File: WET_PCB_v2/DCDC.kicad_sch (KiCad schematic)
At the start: 5 parts, among them Q5 Q_NMOS_GDS, Q6 Q_NMOS_GDS

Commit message: notees
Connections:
- net DCDC_coil_circuit_side: no longer Q5.2 (D), Q6.2 (D)
- net VoutDCDC: now also Q6.2 (D); no longer Q6.3 (S)
- new net Gatedriver/Vs_node: Q5.2 (D), Q6.3 (S)
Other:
- note added: "curr sense points"
- moved on the sheet: Q6
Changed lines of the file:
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@@
+		)
+	)
+	(text "curr sense points"
+		(exclude_from_sim no)
+		(at 82.296 42.926 0)
+		(effects
+			(font
+				(size 1.27 1.27)
+			)
 		)
 	)
@@
 			)
 		)
-	)
-	(junction
-		(at 72.39 43.18)
-		(diameter 0)
-		(color 0 0 0 0)
 	)
 	(junction
@@
 		(color 0 0 0 0)
 	)
-	(junction
-		(at 91.44 43.18)
-		(diameter 0)
-		(color 0 0 0 0)
-	)
 	(wire
 		(pts
@@
 		(pts
 			(xy 72.39 52.07) (xy 72.39 43.18)
-		)
-		(stroke
-			(width 0)
-			(type default)
-		)
-	)
-	(wire
-		(pts
-			(xy 72.39 43.18) (xy 91.44 43.18)
 		)
 		(stroke
@@
 	(symbol
 		(lib_id "Transistor_FET:Q_NMOS_GDS")
-		(at 119.38 45.72 90)
+		(at 119.38 45.72 270)
+		(mirror x)
 		(unit 1)
 		(body_style 1)
@@
 		)
 		(property "Footprint" "Package_TO_SOT_THT:TO-220-3_Vertical"
-			(at 116.84 40.64 0)
-			(hide yes)
-			(show_name no)
+			(at 121.92 40.64 0)
+			(hide yes)
+			(show_name no)

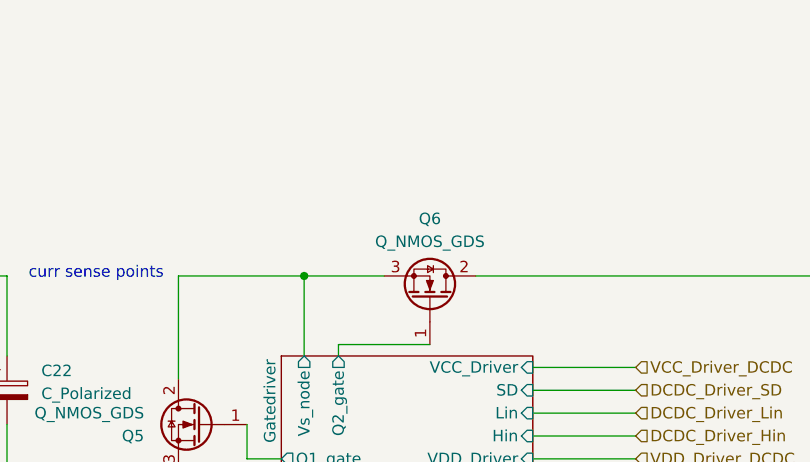
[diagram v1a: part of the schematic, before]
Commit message: redid part of layout inverter
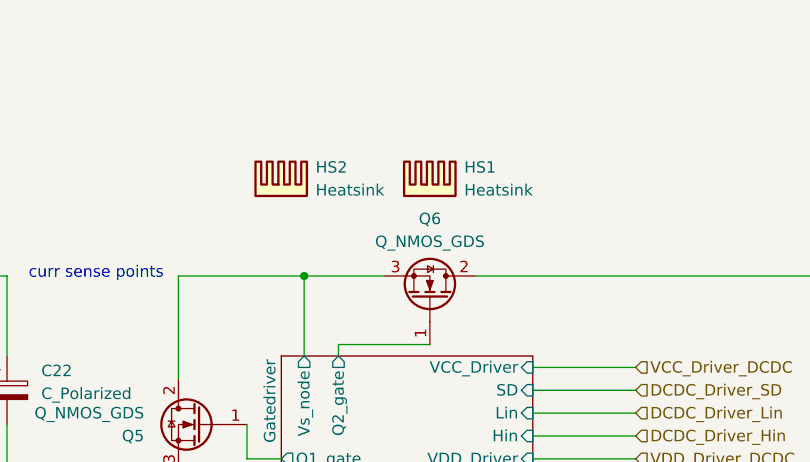
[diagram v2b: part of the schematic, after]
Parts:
- added HS1, HS2: Heatsink, Heatsink:Heatsink_AAVID_Extruded_531002B02100G_34.9x12.7mm_H25.4mm, symbol Mechanical:Heatsink
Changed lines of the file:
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@@
+	)
+	(symbol
+		(lib_id "Mechanical:Heatsink")
+		(at 119.38 34.29 0)
+		(unit 1)
+		(body_style 1)
+		(exclude_from_sim no)
+		(in_bom yes)
+		(on_board yes)
+		(in_pos_files yes)
+		(dnp no)
+		(fields_autoplaced yes)
+		(property "Reference" "HS1"
+			(at 123.19 31.1149 0)
+			(show_name no)
+			(do_not_autoplace no)
+			(effects
+				(font
+					(size 1.27 1.27)
+				)
+				(justify left)
+			)
+		)
+		(property "Value" "Heatsink"
+			(at 123.19 33.6549 0)
+			(show_name no)
+			(do_not_autoplace no)
+			(effects
+				(font
+					(size 1.27 1.27)
+				)
+				(justify left)
+			)
+		)
+		(property "Footprint" "Heatsink:Heatsink_AAVID_Extruded_531002B02100G_34.9x12.7mm_H25.4mm"
+			(at 119.6848 34.29 0)
+			(hide yes)
+			(show_name no)
+			(do_not_autoplace no)
+			(effects
+				(font
+					(size 1.27 1.27)
+				)
+			)
+		)
+		(property "Datasheet" ""
+			(at 119.6848 34.29 0)
+			(hide yes)
+			(show_name no)
+			(do_not_autoplace no)
+			(effects
+				(font
+					(size 1.27 1.27)
+				)
+			)
+		)
+		(property "Description" "Heatsink"
+			(at 119.38 34.29 0)
+			(hide yes)
+			(show_name no)
+			(do_not_autoplace no)
+			(effects
+				(font
+					(size 1.27 1.27)
+				)
+			)
+		)
+		(instances
+			(project "WET_PCB_v2"
+				(path "/13451c35-1666-47d9-9525-8d8125ba1cf3/04007180-46fe-4cf0-9e6f-a7d321798318"
+					(reference "HS1")
+					(unit 1)
+				)
+			)
+		)
 	)
 	(symbol
@@
 					(unit 1)
 				)
+			)
+		)
+	)
+	(symbol
+		(lib_id "Mechanical:Heatsink")
+		(at 102.87 34.29 0)
+		(unit 1)
+		(body_style 1)
+		(exclude_from_sim no)
+		(in_bom yes)
+		(on_board yes)
+		(in_pos_files yes)
+		(dnp no)
+		(fields_autoplaced yes)
+		(property "Reference" "HS2"
+			(at 106.68 31.1149 0)
+			(show_name no)
+			(do_not_autoplace no)
+			(effects
+				(font
+					(size 1.27 1.27)
+				)
+				(justify left)
+			)
+		)
+		(property "Value" "Heatsink"
+			(at 106.68 33.6549 0)
+			(show_name no)
+			(do_not_autoplace no)
+			(effects
+				(font
+					(size 1.27 1.27)
+				)
+				(justify left)
+			)
+		)
+		(property "Footprint" "Heatsink:Heatsink_AAVID_Extruded_531002B02100G_34.9x12.7mm_H25.4mm"
+			(at 103.1748 34.29 0)
+			(hide yes)
+			(show_name no)
+			(do_not_autoplace no)
+			(effects
+				(font
+					(size 1.27 1.27)
+				)
+			)
+		)
+		(property "Datasheet" ""
+			(at 103.1748 34.29 0)
+			(hide yes)
+			(show_name no)
+			(do_not_autoplace no)
+			(effects
+				(font
+					(size 1.27 1.27)
+				)
+			)
+		)
+		(property "Description" "Heatsink"
+			(at 102.87 34.29 0)
+			(hide yes)
+			(show_name no)
+			(do_not_autoplace no)
+			(effects
+				(font
+					(size 1.27 1.27)
+				)
+			)
+		)
+		(instances
+			(project "WET_PCB_v2"
+				(path "/13451c35-1666-47d9-9525-8d8125ba1cf3/04007180-46fe-4cf0-9e6f-a7d321798318"
+					(reference "HS2")
+					(unit 1)
+				)

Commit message: didnt watch the lecture but made progress ig
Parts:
- added C23: C_Polarized, Capacitor_THT:C_Radial_D12.5mm_H20.0mm_P5.00mm, symbol Device:C_Polarized
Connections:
- net GND: now also C23.2
- net VoutDCDC: now also C23.1
- net Gatedriver/Vs_node renamed currsense_FET_side
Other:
- note removed: "curr sense points"
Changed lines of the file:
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@@
-		)
-	)
-	(text "curr sense points"
-		(exclude_from_sim no)
-		(at 82.296 42.926 0)
-		(effects
-			(font
-				(size 1.27 1.27)
-			)
 		)
 	)
@@
 			)
 		)
+	)
+	(junction
+		(at 175.26 64.77)
+		(diameter 0)
+		(color 0 0 0 0)
 	)
 	(junction
@@
 	)
 	(junction
+		(at 175.26 46.99)
+		(diameter 0)
+		(color 0 0 0 0)
+	)
+	(junction
 		(at 175.26 43.18)
 		(diameter 0)
@@
 	(wire
 		(pts
+			(xy 175.26 46.99) (xy 175.26 52.07)
+		)
+		(stroke
+			(width 0)
+			(type default)
+		)
+	)
+	(wire
+		(pts
 			(xy 99.06 63.5) (xy 99.06 59.69)
 		)
@@
 	(wire
 		(pts
+			(xy 175.26 64.77) (xy 175.26 68.58)
+		)
+		(stroke
+			(width 0)
+			(type default)
+		)
+	)
+	(wire
+		(pts
 			(xy 91.44 43.18) (xy 91.44 54.61)
 		)
@@
 	(wire
 		(pts
-			(xy 175.26 43.18) (xy 175.26 52.07)
+			(xy 175.26 43.18) (xy 175.26 46.99)
 		)
 		(stroke
@@
 	(wire
 		(pts
+			(xy 194.31 52.07) (xy 194.31 46.99)
+		)
+		(stroke
+			(width 0)
+			(type default)
+		)
+	)
+	(wire
+		(pts
 			(xy 119.38 50.8) (xy 109.22 50.8)
 		)
@@
 	(wire
 		(pts
+			(xy 194.31 64.77) (xy 175.26 64.77)
+		)
+		(stroke
+			(width 0)
+			(type default)
+		)
+	)
+	(wire
+		(pts
 			(xy 91.44 64.77) (xy 91.44 68.58)
 		)
@@
 	(wire
 		(pts
-			(xy 175.26 59.69) (xy 175.26 68.58)
+			(xy 175.26 59.69) (xy 175.26 64.77)
+		)
+		(stroke
+			(width 0)
+			(type default)
+		)
+	)
+	(wire
+		(pts
+			(xy 194.31 46.99) (xy 175.26 46.99)
+		)
+		(stroke
+			(width 0)
+			(type default)
+		)
+	)
+	(wire
+		(pts
+			(xy 194.31 59.69) (xy 194.31 64.77)
 		)
 		(stroke
@@
 		)
 	)
+	(hierarchical_label "currsense_FET_side"
+		(shape input)
+		(at 91.44 43.18 90)
+		(effects
+			(font
+				(size 1.27 1.27)
+			)
+			(justify left)
+		)
+	)
 	(hierarchical_label "Vin_DCDC+"
 		(shape input)
@@
 			)
 			(justify right)
+		)
+	)
+	(hierarchical_label "currsense_cap_side"
+		(shape input)
+		(at 72.39 43.18 90)
+		(effects
+			(font
+				(size 1.27 1.27)
+			)
+			(justify left)
 		)
 	)
@@
 					(unit 1)
 				)
+			)
+		)
+	)
+	(symbol
+		(lib_id "Device:C_Polarized")
+		(at 194.31 55.88 0)
+		(unit 1)
+		(body_style 1)
+		(exclude_from_sim no)
+		(in_bom yes)
+		(on_board yes)
+		(in_pos_files yes)
+		(dnp no)
+		(fields_autoplaced yes)
+		(property "Reference" "C23"
+			(at 198.12 53.7209 0)
+			(show_name no)
+			(do_not_autoplace no)
+			(effects
+				(font
+					(size 1.27 1.27)
+				)
+				(justify left)
+			)
+		)
+		(property "Value" "C_Polarized"
+			(at 198.12 56.2609 0)
+			(show_name no)
+			(do_not_autoplace no)
+			(effects
+				(font
+					(size 1.27 1.27)
+				)
+				(justify left)
+			)
+		)
+		(property "Footprint" "Capacitor_THT:C_Radial_D12.5mm_H20.0mm_P5.00mm"
+			(at 195.2752 59.69 0)
+			(hide yes)
+			(show_name no)
+			(do_not_autoplace no)
+			(effects
+				(font
+					(size 1.27 1.27)
+				)
+			)
+		)
+		(property "Datasheet" ""
+			(at 194.31 55.88 0)
+			(hide yes)
+			(show_name no)
+			(do_not_autoplace no)
+			(effects
+				(font
+					(size 1.27 1.27)
+				)
+			)
+		)
+		(property "Description" "Polarized capacitor"
+			(at 194.31 55.88 0)
+			(hide yes)
+			(show_name no)
+			(do_not_autoplace no)
+			(effects
+				(font
+					(size 1.27 1.27)
+				)
+			)
+		)
+		(pin "1"
+		)
+		(pin "2"
+		)
+		(instances
+			(project "WET_PCB_v2"
+				(path "/13451c35-1666-47d9-9525-8d8125ba1cf3/04007180-46fe-4cf0-9e6f-a7d321798318"
+					(reference "C23")
+					(unit 1)
+				)
